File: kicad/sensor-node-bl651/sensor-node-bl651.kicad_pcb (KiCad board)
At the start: 2 copper layers, 18.2 x 54.5 mm, 35 parts, among them P1 TPS61098x, U1 DMP2008UFG-7, U2 DMP2008UFG-7, U3 LSM303AGR, Y1 32.768 kHz

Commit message: apply finishing touches
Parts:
- L1: value 4.7µF -> 4.7µH; footprint Capacitor_SMD:C_0603_1608Metric -> Inductor_SMD:L_1008_2520Metric
- moved P1 0.75 mm to (149.2, 78.5)
- moved L1 0.60 mm to (148.8, 75.2)
- moved C4 0.45 mm to (147.4, 78.8)
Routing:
- net GND: track 29.5 -> 32.4 mm, vias 15 -> 14
- net /mcu/VDD: track 86.6 -> 85.8 mm
- net /mcu/V_sen2: track 22.7 -> 22.0 mm

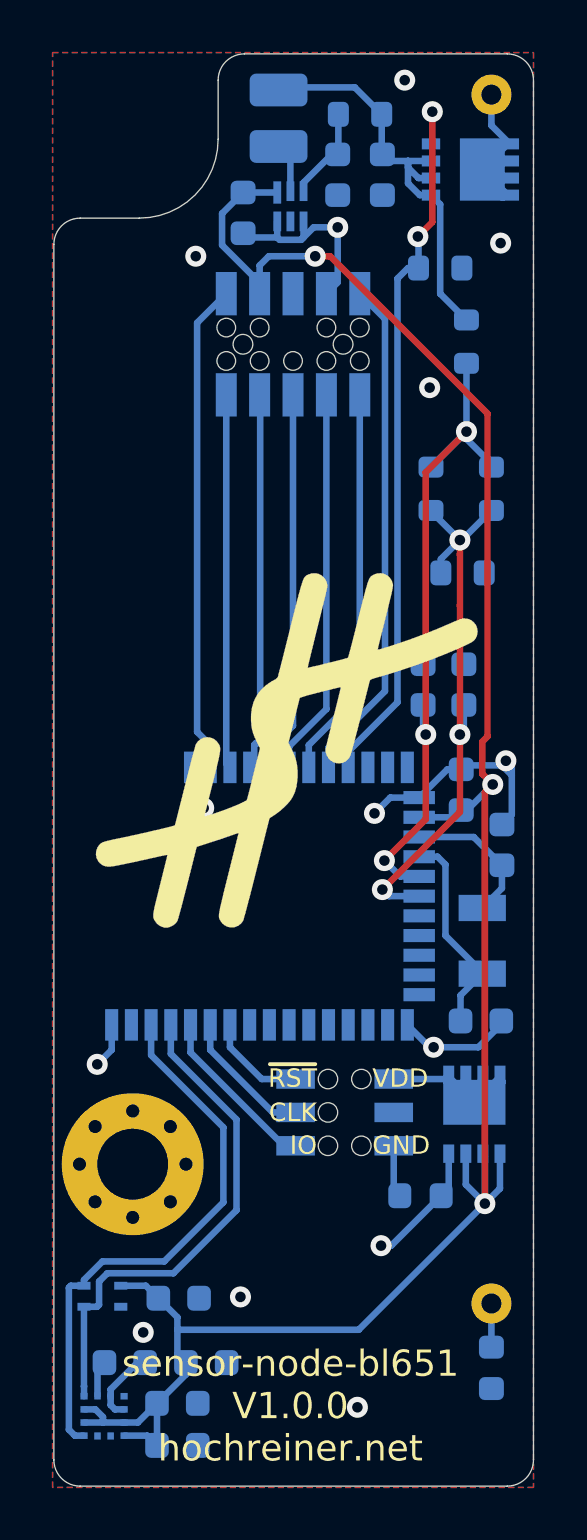
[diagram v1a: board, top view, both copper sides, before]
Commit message: add TPS6031x
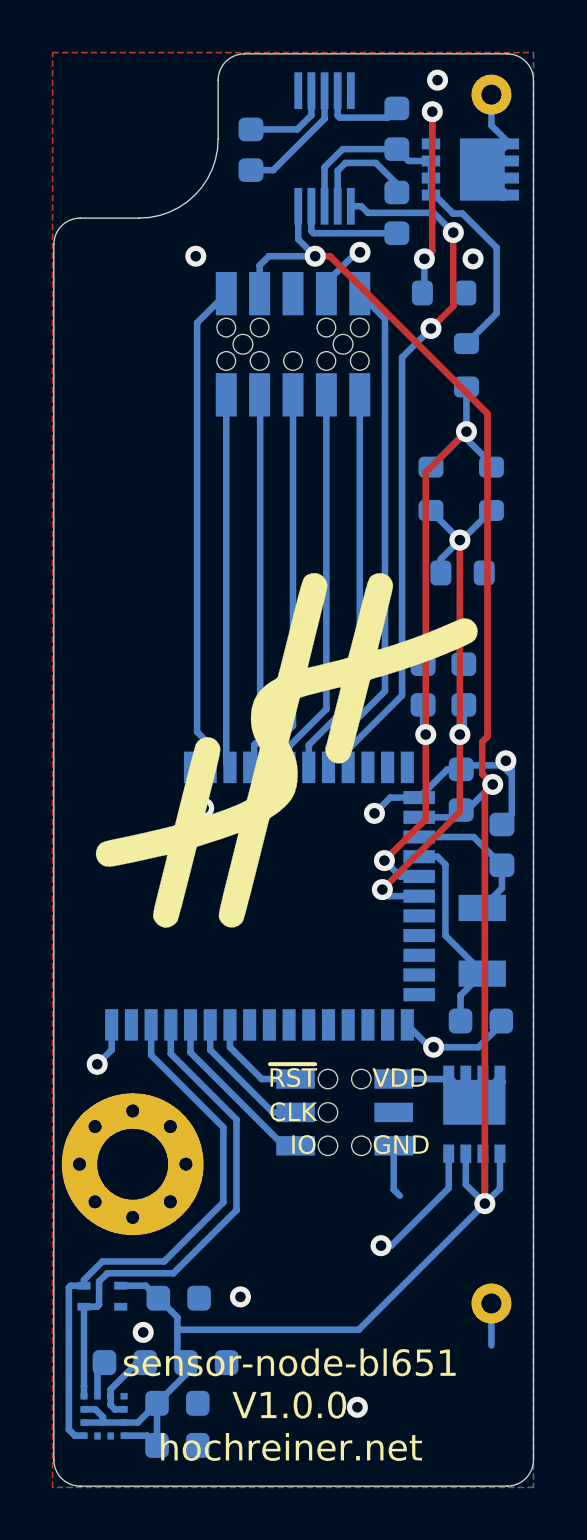
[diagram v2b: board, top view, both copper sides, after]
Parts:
- removed F1, F3: Polyfuse, Fuse:Fuse_0603_1608Metric
- removed L1: 4.7µH, Inductor_SMD:L_1008_2520Metric
- removed P1: TPS61098x, HH_TexasInstruments:TPS61098x
- removed R3: 400 0603, Resistor_SMD:R_0603_1608Metric
- added T1: TPS6031x, Package_SO:MSOP-10_3x3mm_P0.5mm, B.Cu at (150.6, 76.3)
- C2, C4: value 10µF 0603 -> 1µF X7R 0603
- C3: value 0.1µF 0603 -> 1µF X7R 0603
- moved C3 2.68 mm to (153.3, 78.8)
- moved C4 2.42 mm to (147.8, 76.4), turned to 90 degrees
- moved C2 1.83 mm to (153.3, 75.6), turned to 90 degrees
- moved R6 0.96 mm to (155.1, 81.8)
- moved R4 0.90 mm to (155.9, 84.6)
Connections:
- BL1 pad 31: /mcu/UVLO -> /mcu/~SNOOZE
- BT1 pad 2: Net-(BT1-Pad2) -> GND
- C3 pad 2: GND -> Net-(C3-Pad2)
- C4 pad 1: /mcu/VDD -> Net-(C4-Pad1)
- C4 pad 2: GND -> Net-(C4-Pad2)
- R6 pad 1: /mcu/UVLO -> Net-(R6-Pad1)
- S2 pad 1: Net-(F3-Pad1) -> GND
- U2 pad 4: /mcu/UVLO -> Net-(R6-Pad1)
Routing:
- net /mcu/UVLO: track 27.8 -> 0.00 mm, vias 2 -> 0
- net /mcu/~SNOOZE: track 0.00 -> 26.3 mm, vias 0 -> 2
- net Net-(R6-Pad1): track 0.00 -> 8.30 mm, vias 0 -> 2
- net Net-(C4-Pad1): track 0.00 -> 4.68 mm
- net Net-(C3-Pad2): track 0.00 -> 4.22 mm
- net /mcu/VDD: track 85.8 -> 81.9 mm
- net Net-(C4-Pad2): track 0.00 -> 3.46 mm
- net Net-(F3-Pad1): track 2.00 -> 0.00 mm
- net Net-(L1-Pad2): track 1.89 -> 0.00 mm
- net Net-(BT1-Pad2): track 1.60 -> 0.00 mm
- net GND: track 32.4 -> 33.6 mm, vias 14 -> 13
- net /mcu/V_BAT: track 15.9 -> 14.8 mm
- net /mcu/V_sen1: track 26.6 -> 25.7 mm
- net Net-(C3-Pad1): track 3.61 -> 4.38 mm

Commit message: remove second measurement point
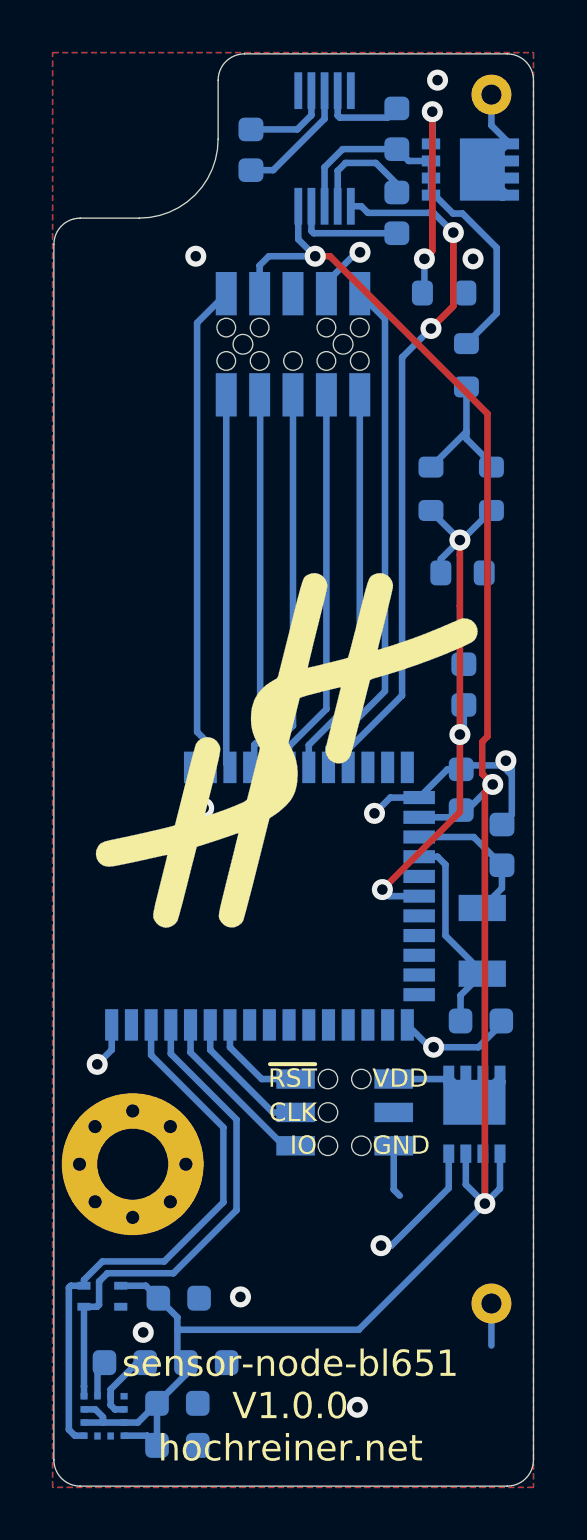
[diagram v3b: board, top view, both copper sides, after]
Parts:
- removed C6: 0.1µF 0603 16V, Capacitor_SMD:C_0603_1608Metric
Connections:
- net /mcu/V_sen2 renamed /mcu/V_sen
- BL1 pad 23: /mcu/V_sen1 -> (no net)
- R1 pad 2: /mcu/V_sen1 -> Net-(R1-Pad2)
- R4 pad 1: /mcu/V_sen1 -> Net-(R1-Pad2)
- R5 pad 2: /mcu/V_sen1 -> Net-(R1-Pad2)
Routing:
- net /mcu/V_sen1: track 25.7 -> 0.00 mm, vias 3 -> 0
- net Net-(R1-Pad2): track 0.00 -> 5.35 mm

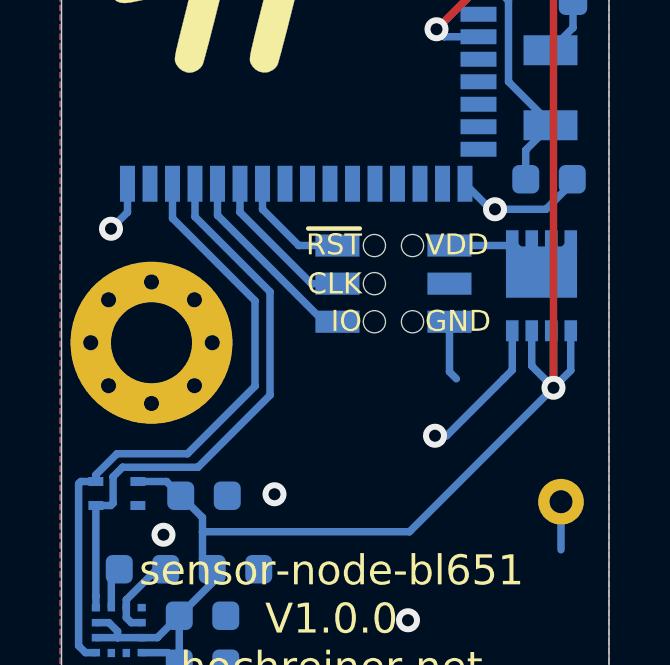
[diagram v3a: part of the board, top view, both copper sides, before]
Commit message: update swd footprint
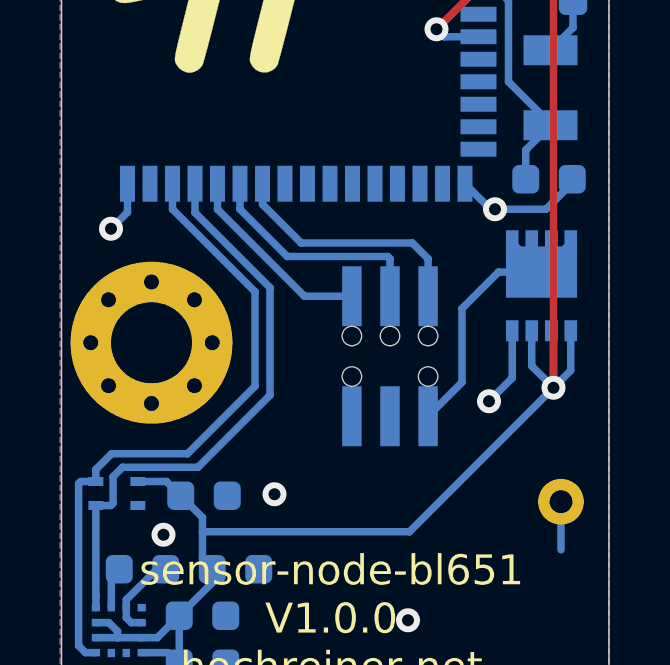
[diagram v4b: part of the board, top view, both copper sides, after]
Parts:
- S2: footprint HH_Hochreiner:swd_connector -> HH_Hochreiner:SWD_BD050-06-A-0-0500-L-D
- moved S2 2.42 mm to (151.2, 115.5), turned to 0 degrees
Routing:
- net Net-(S2-Pad5): track 7.42 -> 12.5 mm
- net /mcu/~RESET: track 3.85 -> 8.21 mm
- net GND: track 33.6 -> 29.5 mm
- net /mcu/SWDCLK: track 5.18 -> 7.78 mm

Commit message: update sensor connector
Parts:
- SC1: footprint HH_Hochreiner:sensor_connector_M50-3150542R_keyed -> HH_Hochreiner:Sensor-Connector_BD050-10-A-0-0500-L-D

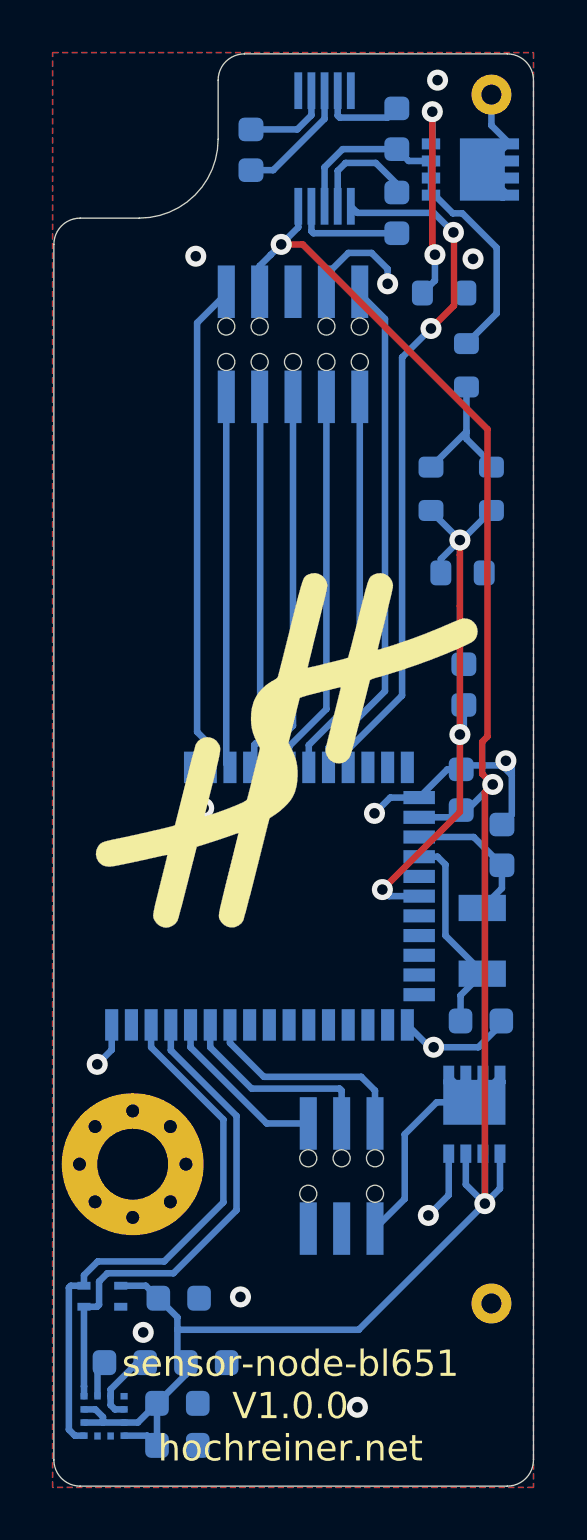
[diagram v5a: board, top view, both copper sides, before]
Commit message: update sensor and swd connectors
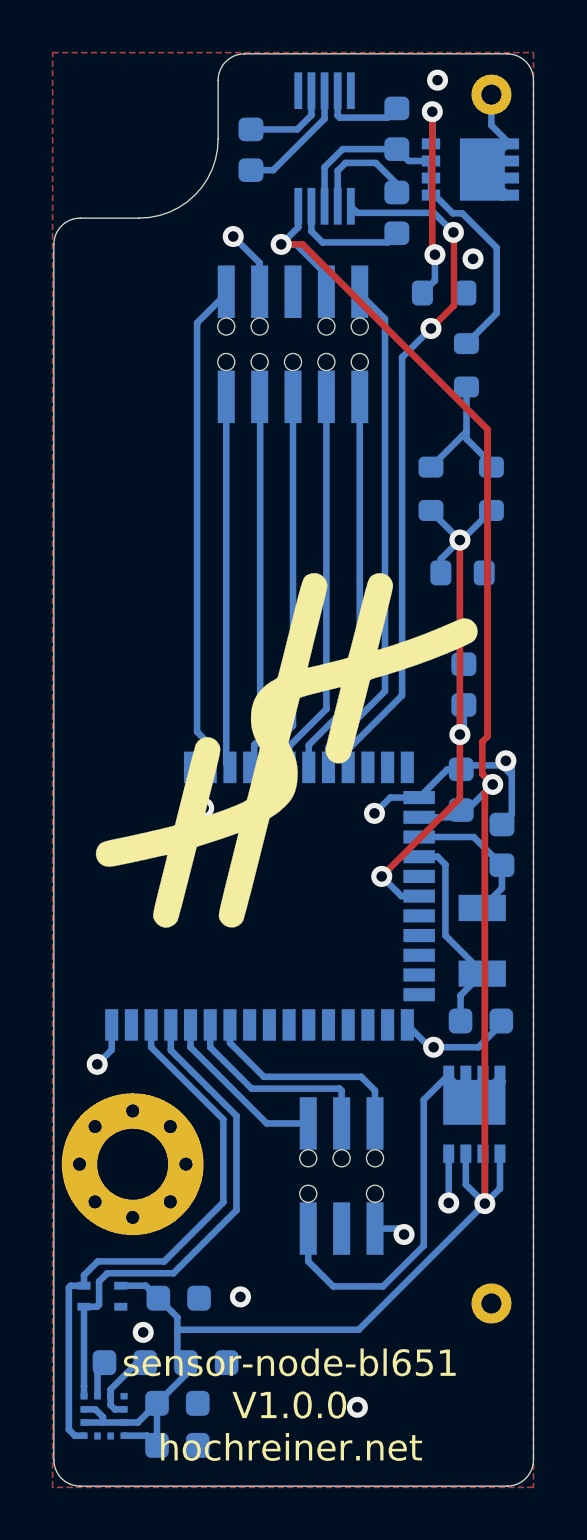
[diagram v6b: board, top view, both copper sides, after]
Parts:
- S2: value swd_connector -> swd_connector_keyed
- turned S2 to 180 degrees
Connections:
- S2 pad 2: /mcu/SWDIO -> /mcu/~RESET
- S2 pad 6: /mcu/~RESET -> /mcu/SWDIO
- SC1 pad 3: /mcu/VDD -> GND
- SC1 pad 7: GND -> /mcu/VDD
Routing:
- net Net-(S2-Pad5): track 12.5 -> 18.8 mm
- net GND: track 30.0 -> 28.7 mm
- net /mcu/VDD: track 81.5 -> 82.1 mm
